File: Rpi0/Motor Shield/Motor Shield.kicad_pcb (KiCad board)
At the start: 2 copper layers, 29.8 x 64.8 mm, 27 parts, among them J1 Conn_01x02, J2 Conn_01x02, J3 Conn_01x02, J4 Conn_01x02, Q1 Q_PMOS_GDSD, U1 IFX9201, U2 IFX9201, U3 PIC16(L)F1509-I/SO, U4 RPi0, U5 LD1117S33TR_SOT223

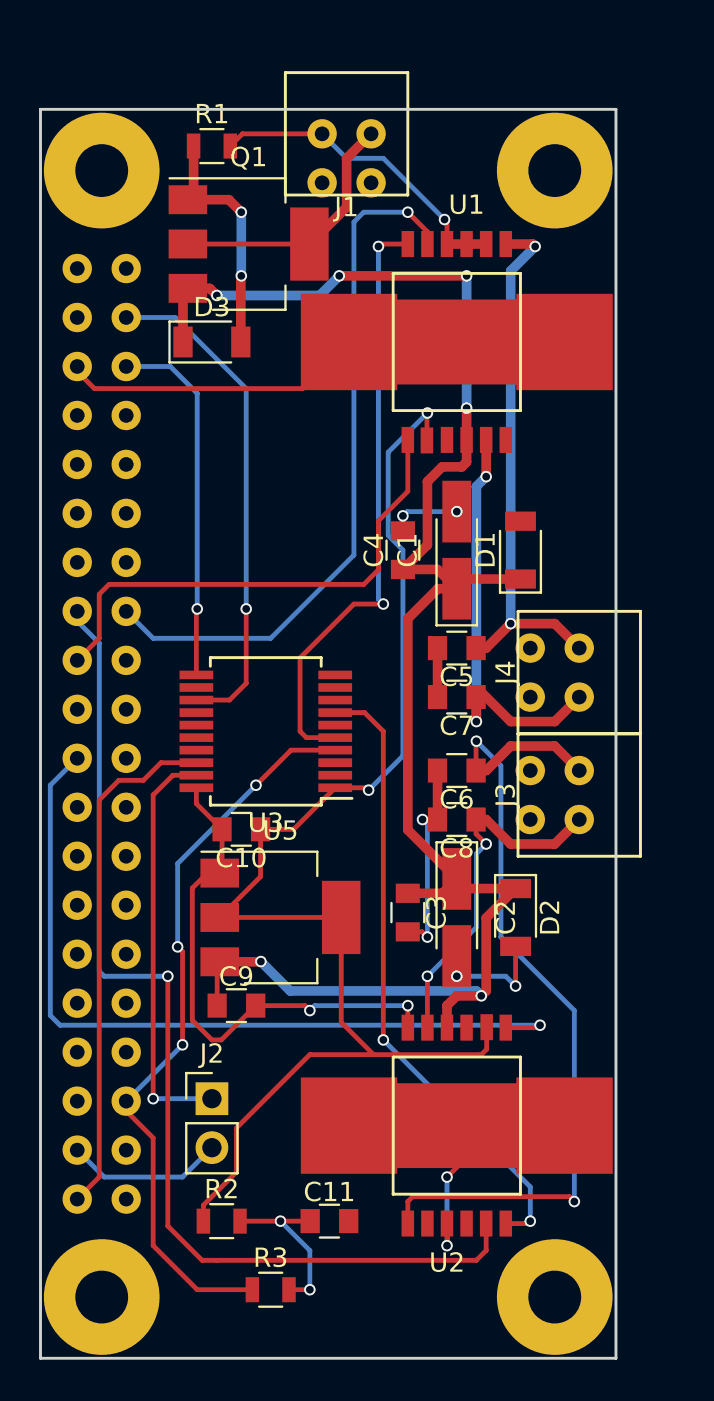
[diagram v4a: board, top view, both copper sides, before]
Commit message: Removed unnecessary 3.3V regulator. Added encoder pins with 5v regulator
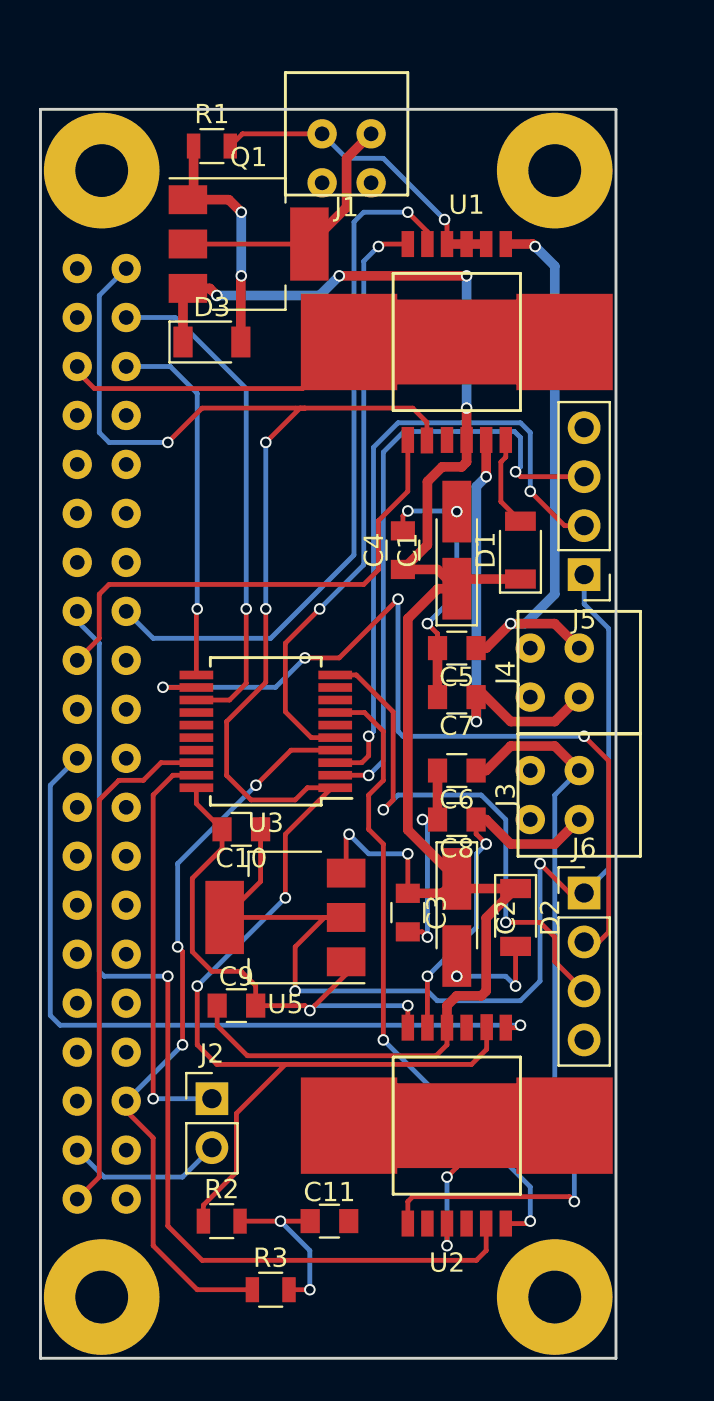
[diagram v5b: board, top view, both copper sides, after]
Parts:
- added J5: Conn_01x04, Pin_Headers:Pin_Header_Straight_1x04_Pitch2.54mm, F.Cu at (170.4, 94.0)
- added J6: Conn_01x04, Pin_Headers:Pin_Header_Straight_1x04_Pitch2.54mm, F.Cu at (170.4, 110.5)
- U5: value LD1117S33TR_SOT223 -> LD1117S50TR_SOT223
- moved U5 0.25 mm to (154.9, 111.8), turned to 180 degrees
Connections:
- C10 pad 1: +3V3 -> +5V
- U3 pad 10: Net-(U3-Pad10) -> B2
- U3 pad 12: Net-(U3-Pad12) -> A2
- U3 pad 2: Net-(U3-Pad2) -> B1
- U3 pad 3: Net-(U3-Pad3) -> A1
- U4 pad 1: Net-(U4-Pad1) -> +3V3
- U5 pad 2: +3V3 -> +5V
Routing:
- net +5V: track 0.00 -> 57.6 mm, vias 0 -> 2
- net A2: track 0.00 -> 44.6 mm, vias 0 -> 4
- net A1: track 0.00 -> 33.4 mm, vias 0 -> 2
- net B1: track 0.00 -> 32.0 mm, vias 0 -> 2
- net +3V3: track 70.3 -> 98.8 mm, vias 2 -> 5
- net B2: track 0.00 -> 27.9 mm, vias 0 -> 2
- net BAT-: track 90.6 -> 103.3 mm, vias 11 -> 12
- net BAT-PROT+: track 91.7 -> 97.4 mm
- net OUT4: track 43.9 -> 39.7 mm, vias 2 -> 1
- net DIR2: track 41.4 -> 39.3 mm
- net OUT2: track 28.1 -> 29.4 mm
- net PWM2: track 32.8 -> 33.4 mm
- net PWM1: track 31.5 -> 30.8 mm

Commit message: Added pins option to power the raspberry pi from the battery
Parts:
- added J7: Conn_01x02, Pin_Headers:Pin_Header_Straight_1x02_Pitch2.54mm, F.Cu at (156.2, 89.2)
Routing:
- net +5V: track 57.6 -> 87.2 mm, vias 2 -> 4
- net Net-(J7-Pad1): track 0.00 -> 25.3 mm

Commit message: Update to Kicad 5.0
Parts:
- J1: value Conn_01x02 -> Screw_Terminal_01x02
- J2: value Conn_01x02 -> Conn_02x01
- J3: value Conn_01x02 -> Conn_02x01; footprint Rob:PCB_Terminal_1725656 -> Pin_Headers:Pin_Header_Straight_1x02_Pitch2.54mm
- J4: value Conn_01x02 -> Screw_Terminal_01x02; footprint Rob:PCB_Terminal_1725656 -> TerminalBlock_Phoenix:TerminalBlock_Phoenix_MPT-0,5-2-2.54_1x02_P2.54mm_Horizontal
- J5: value Conn_01x04 -> Screw_Terminal_01x02; footprint Pin_Headers:Pin_Header_Straight_1x04_Pitch2.54mm -> TerminalBlock_Phoenix:TerminalBlock_Phoenix_MPT-0,5-2-2.54_1x02_P2.54mm_Horizontal
- J6: value Conn_01x04 -> Conn_01x04_Female; footprint Pin_Headers:Pin_Header_Straight_1x04_Pitch2.54mm -> Socket_Strips:Socket_Strip_Straight_1x04_Pitch2.54mm
- J7: value Conn_01x02 -> Conn_01x04_Female; footprint Pin_Headers:Pin_Header_Straight_1x02_Pitch2.54mm -> Socket_Strips:Socket_Strip_Straight_1x04_Pitch2.54mm
- U3: value PIC16(L)F1509-I/SO -> PIC16F1509-ISS
- moved J7 25.6 mm to (170.4, 110.5)
- moved J3 19.6 mm to (156.2, 91.7), turned to 180 degrees
- moved J6 16.5 mm to (170.4, 94.0), turned to 180 degrees
- moved J4 5.09 mm to (169.9, 104.1), turned to 270 degrees
- moved J5 3.84 mm to (169.9, 97.8), turned to 270 degrees
- moved J2 2.54 mm to (151.1, 123.7), turned to 180 degrees
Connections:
- J2 pad 1: Net-(J2-Pad1) -> ICSP_DAT
- J2 pad 2: ICSP_DAT -> Net-(J2-Pad2)
- J3 pad 1: OUT3 -> +5V
- J3 pad 2: OUT4 -> Net-(J3-Pad2)
- J4 pad 1: OUT1 -> OUT4
- J4 pad 2: OUT2 -> OUT3
- J5 pad 1: +5V -> OUT2
- J5 pad 2: A1 -> OUT1
- J6 pad 2: A2 -> A1
- J6 pad 3: B2 -> B1
- J7 pad 1: Net-(J7-Pad1) -> +5V
- J7 pad 2: +5V -> A2
- U3 pad 19: Net-(J2-Pad1) -> Net-(J2-Pad2)
- U4 pad 2: Net-(J7-Pad1) -> Net-(J3-Pad2)
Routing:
- net Net-(J7-Pad1): track 25.3 -> 0.00 mm
- net Net-(J3-Pad2): track 0.00 -> 25.3 mm
- net Net-(J2-Pad2): track 0.00 -> 21.5 mm, vias 0 -> 1
- net Net-(J2-Pad1): track 21.5 -> 0.00 mm, vias 1 -> 0
- net BAT-: track 103.3 -> 109.4 mm
- net A2: track 44.6 -> 45.2 mm

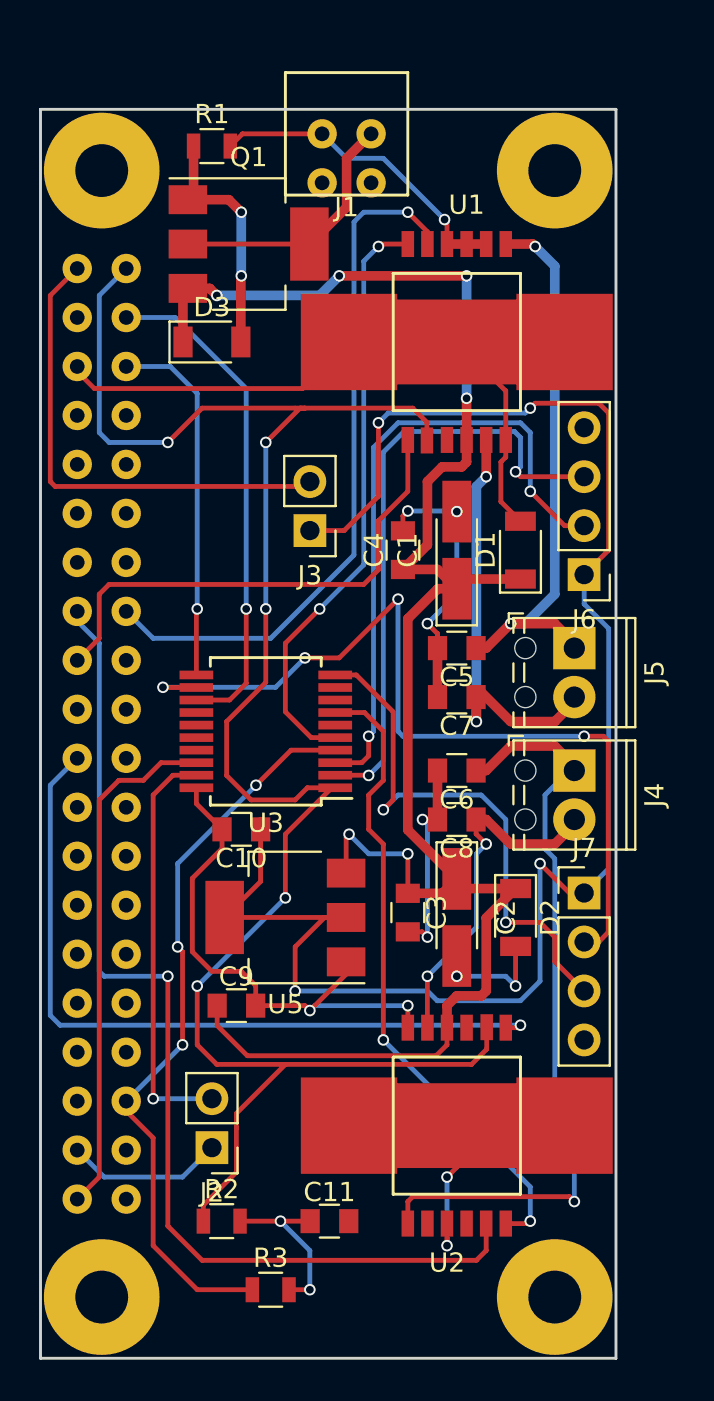
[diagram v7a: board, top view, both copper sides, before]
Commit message: Upgrade to Kicad 5.0
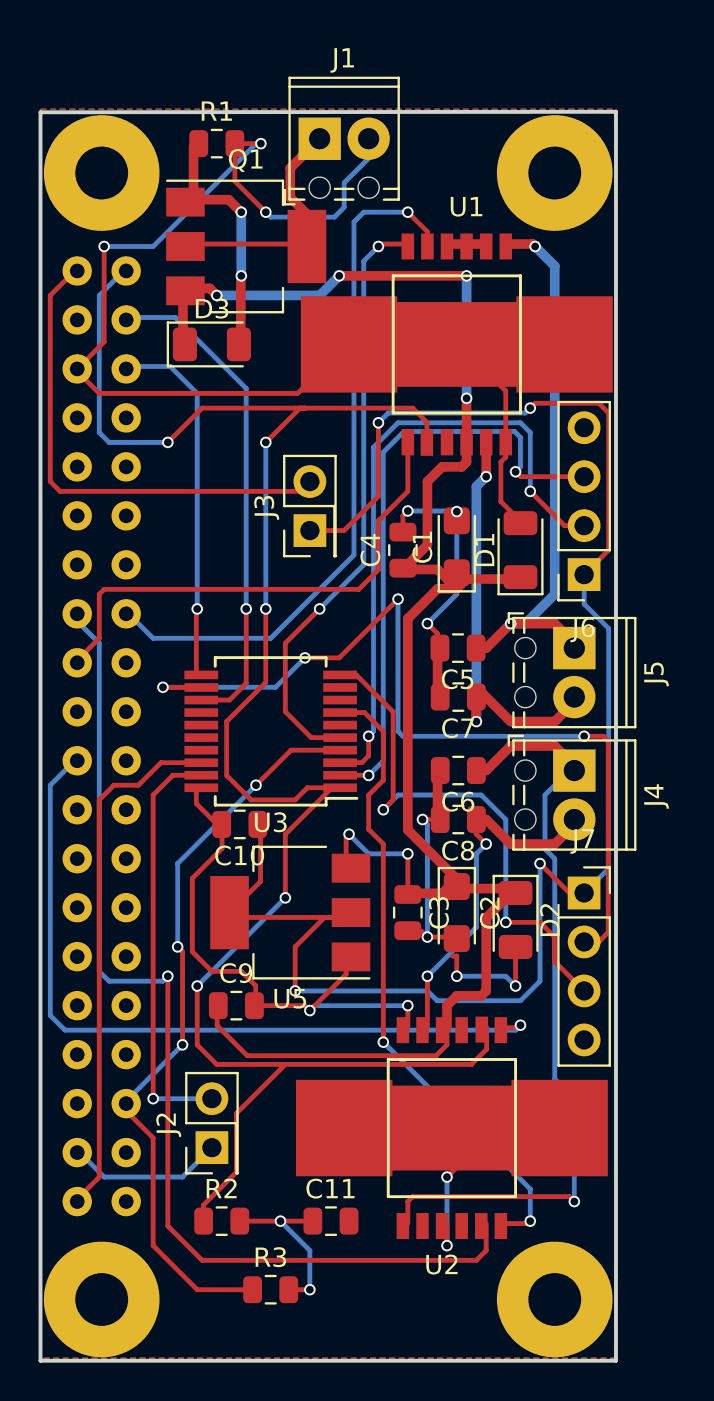
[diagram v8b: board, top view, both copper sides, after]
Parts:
- C1, C2: footprint Capacitors_Tantalum_SMD:CP_Tantalum_Case-A_EIA-3216-18_Hand -> Capacitor_Tantalum_SMD:CP_EIA-3216-18_Kemet-A
- C10, C11, C3, C4, C5, C6, C7, C8, C9: footprint Capacitors_SMD:C_0805 -> Capacitor_SMD:C_0805_2012Metric
- D1, D2, D3: footprint Diodes_SMD:D_1206 -> Diode_SMD:D_1206_3216Metric
- J1: footprint Rob:PCB_Terminal_1725656 -> TerminalBlock_Phoenix:TerminalBlock_Phoenix_MPT-0,5-2-2.54_1x02_P2.54mm_Horizontal
- J2, J3: footprint Pin_Headers:Pin_Header_Straight_1x02_Pitch2.54mm -> Connector_PinHeader_2.54mm:PinHeader_2x01_P2.54mm_Vertical
- J6, J7: footprint Socket_Strips:Socket_Strip_Straight_1x04_Pitch2.54mm -> Connector_PinSocket_2.54mm:PinSocket_1x04_P2.54mm_Vertical
- Q1: footprint TO_SOT_Packages_SMD:SOT-223 -> Package_TO_SOT_SMD:SOT-223
- R1, R2, R3: footprint Resistors_SMD:R_0805 -> Resistor_SMD:R_0805_2012Metric
- U1, U2: value IFX9201 -> IFX9201SG; footprint Rob:IFX9201 -> Rob-5.0:IFX9201SG
- U3: footprint Housings_SSOP:SSOP-20_5.3x7.2mm_Pitch0.65mm -> Package_SO:SSOP-20_5.3x7.2mm_P0.65mm
- U4: value RPi0 -> RPI0-Template; footprint Rob:RPi0_Template -> Rob-5.0:RPi0_Template
- U5: footprint TO_SOT_Packages_SMD:SOT-223-3_TabPin2 -> Package_TO_SOT_SMD:SOT-223-3_TabPin2
- moved J1 1.42 mm to (156.7, 71.4), turned to 0 degrees
- moved U5 0.36 mm to (155.2, 111.5)
- moved U2 0.28 mm to (163.6, 122.7)
- moved R1 0.28 mm to (151.4, 71.6)
- moved C10 0.27 mm to (152.6, 106.9)
- moved C2 0.25 mm to (163.8, 111.5)
- moved U3 0.25 mm to (154.2, 102.1)
- moved Q1 0.18 mm to (152.9, 77.0)
- moved C1 0.17 mm to (163.8, 92.5)
- moved D2 0.13 mm to (166.9, 111.9)
- moved U4 0.13 mm to (152.4, 99.8)
- moved D3 0.13 mm to (151.1, 82.0)
- moved U1 0.13 mm to (163.8, 82.0)
- moved C11 0.08 mm to (157.3, 127.5)
- moved C6 0.08 mm to (163.9, 104.1)
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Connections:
- U1 pad 8: BAT- -> Net-(U1-Pad8)
- U1 pad 9: BAT- -> Net-(U1-Pad9)
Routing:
- net BAT-: track 109.4 -> 127.9 mm, vias 12 -> 14
